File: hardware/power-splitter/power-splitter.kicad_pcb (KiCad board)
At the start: 2 copper layers, 32 x 25 mm, 6 parts, among them J1 Conn_Power, J3 Conn_01x02_Female, J4 Conn_01x02_Female

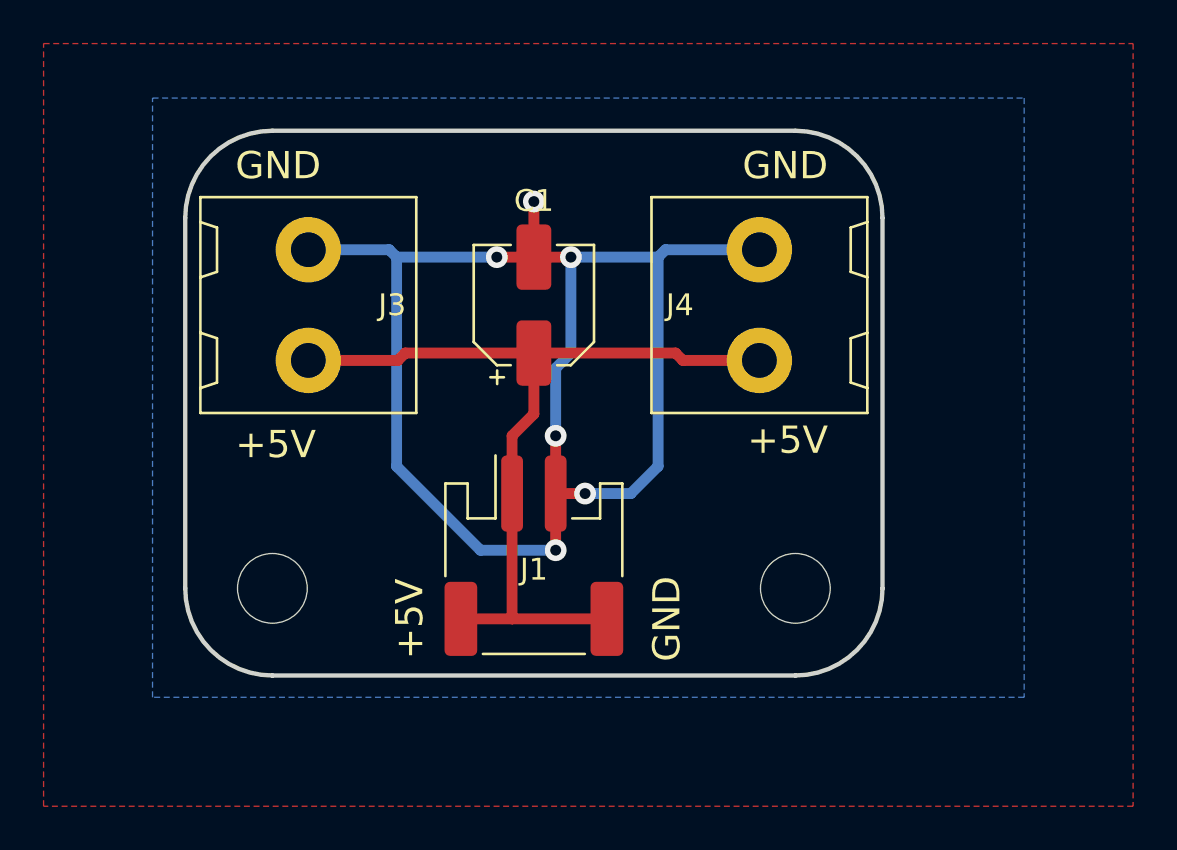
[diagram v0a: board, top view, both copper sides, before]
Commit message: Update all to Kicad 6
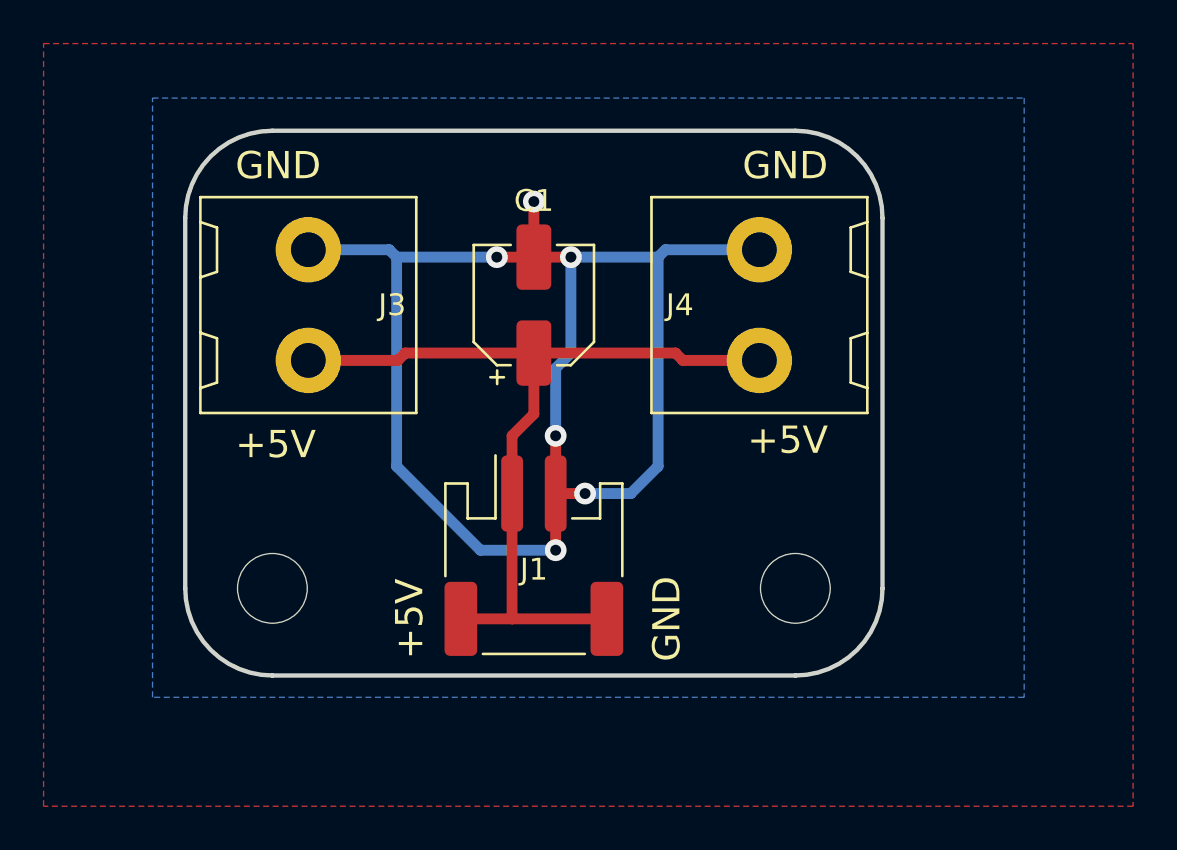
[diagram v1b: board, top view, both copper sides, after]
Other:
- net class Default removed
